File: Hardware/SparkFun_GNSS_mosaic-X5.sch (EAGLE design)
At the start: 68 parts, among them J3 MICROSD, J5 USB Female Type C Connector, U1 MOSAIC-X5X5, U2 SN74AHC1G125DBVR, U5 AP2112K-3.3V

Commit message: Route board.
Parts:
- added R1: 10k, SparkFun-Resistors:10KOHM-0603-1/10W-1%
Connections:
- net PPS_18V renamed PPS_1V8
- new net N$5: J3.DAT3/!CS!, R1.1
- net 3.3V: now also R1.2
- net D+: now also D1.IO4; no longer D1.IO3
- net D-: now also D1.IO3; no longer D1.IO4
- net VIN: now also J7.3; no longer J7.4
- net V_USB: now also J7.4; no longer J7.3
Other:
- note added: "Septentrio mosaic-X5"
- note removed: "Can GP and LOG LEDs be directly driven from module?"
- note removed: "Does the log button have a pull up?"
- moved on the sheet: C1, C18, C19, C20, C3, C4, C5, D10, E1, E2, FB1, J3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

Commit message: Add jumper to ant voltage. Add production panel.
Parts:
- removed C1: 0.1uF, SparkFun-Capacitors:0.1UF-0603-25V-5%
- removed J10: (no value), SparkFun-Connectors:CONN_06NO_SILK_FEMALE_PTH
- removed L1: 39nH, SparkFun-Coils:39NH-0603
- added ANT_V: JUMPER-SMT_3_1-NC_TRACE_SILK, SparkFun-Jumpers:JUMPER-SMT_3_1-NC_TRACE_SILK
- added D2: WHITE, SparkFun-LED:LED-WHITE0603
- added GP2: JUMPER-SMT_2_NC_TRACE_SILK, SparkFun-Jumpers:JUMPER-SMT_2_NC_TRACE_SILK
- added J6: (no value), SparkFun-Connectors:CONN_07NO_SILK
- added Q9: 20V/0.2A/8MHz/1.2Ω/1Vth, SparkFun-DiscreteSemi:MOSFET-NCH-RE1C00UNTL
- added R46, R47: 2.2k, SparkFun-Resistors:2.2KOHM-0603-1/10W-1%
- added R6, R7: 169K, SparkFun-Resistors:169KOHM
- added R9: 1k, SparkFun-Resistors:1KOHM-0603-1/10W-1%
- R11, R4: value 1k -> 2.2k; device SparkFun-Resistors:1KOHM-0603-1/10W-1% -> SparkFun-Resistors:2.2KOHM-0603-1/10W-1%
- R12: value 1k -> 330; device SparkFun-Resistors:1KOHM-0603-1/10W-1% -> SparkFun-Resistors:330OHM-0603-1/10W-1%
- U1: device Septentrio_Mosaic:MOSAIC-X5X5 -> Septentriom_mosaic-X5:MOSAIC-X5X5
- renumbered GP to GP1
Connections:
- net GP_LED renamed PVT_LED
- removed net ANT_VCC: C1.1, L1.2
- new net ANT_V: ANT_V.2, C3.1, FB1.1
- new net ICM-20948-LV_#_1.8V: Q9.G, R46.2
- new net N$6: R6.1, U1.EVENTA
- new net N$7: R7.1, U1.EVENTB
- new net N$8: D2.A, R9.1
- new net N$9: GP2.1, R9.2
- new net PPS_3: Q9.D, R47.1, U2U1.A
- new net RTK_LED: GP2.2, J6.3, U1.GP_LED2
- net 3.3V: now also ANT_V.1, R47.2
- net 5V: now also ANT_V.3; no longer C3.1, FB1.1
- net EVENTA: now also J6.6, R6.2; no longer J10.5, U1.EVENTA
- net EVENTB: now also J6.7, R7.2; no longer J10.6, U1.EVENTB
- net GND: now also D2.C, U1.ANT_2; no longer C1.2
- net GP1: now also J6.1; no longer J10.1
- net GP2: now also J6.2; no longer J10.2
- net GPS_ANT1: no longer L1.1
- net LOG_BTN: now also J6.4; no longer J10.3
- net PPS_1V8: now also Q9.S, R46.1; no longer U2U1.A
- net PPS_3V3: now also J6.5; no longer J10.4
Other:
- note added: "1.8V Input protected by 169k/200k divider"
- note added: "If using single external 3.3V source, move jumper to power antenna with 3.3V."
- note added: "VMax: 6V"
- moved on the sheet: C18, C19, C20, D10, E1, E2, J3, R1, R2, R3, R8, S1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

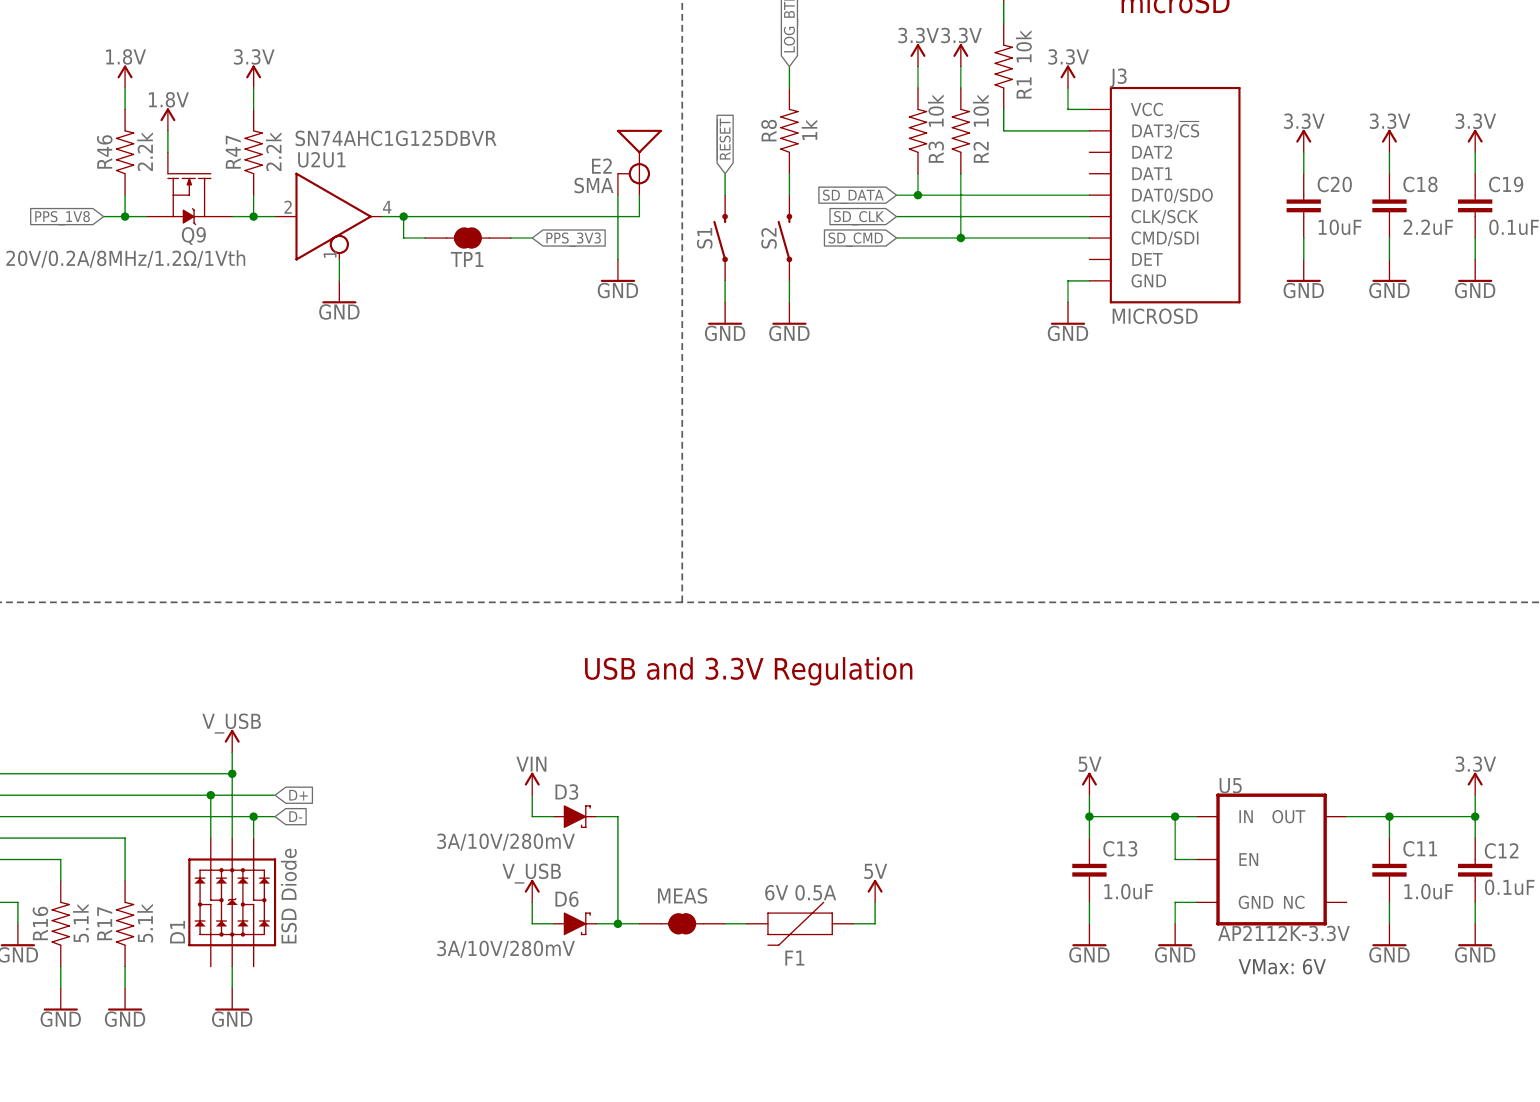
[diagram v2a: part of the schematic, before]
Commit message: Fixed tCream on mosaic pin 1.
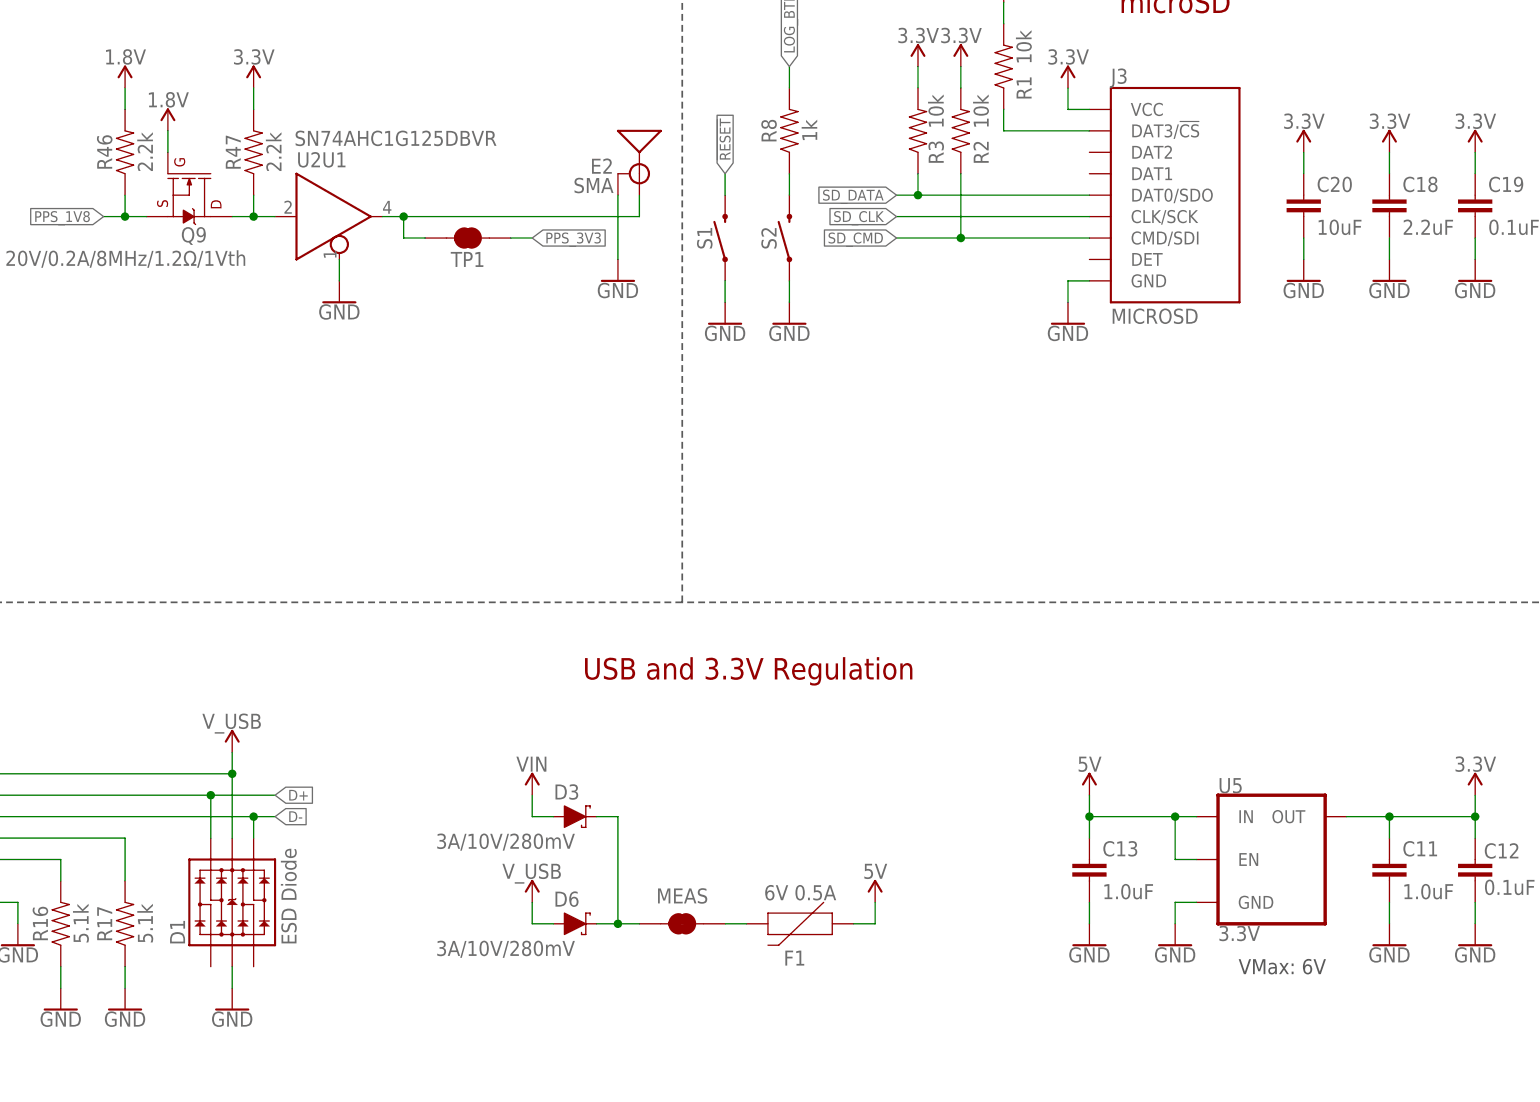
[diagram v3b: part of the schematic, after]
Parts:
- Q9: device SparkFun-DiscreteSemi:MOSFET-NCH-RE1C00UNTL -> SparkFun-DiscreteSemi:MOSFET-NCH-RE1C002UNTCL
- U1: device Septentriom_mosaic-X5:MOSAIC-X5X5 -> Septentrio_mosaic-X5:MOSAIC-X5X5
- U5: value AP2112K-3.3V -> 3.3V

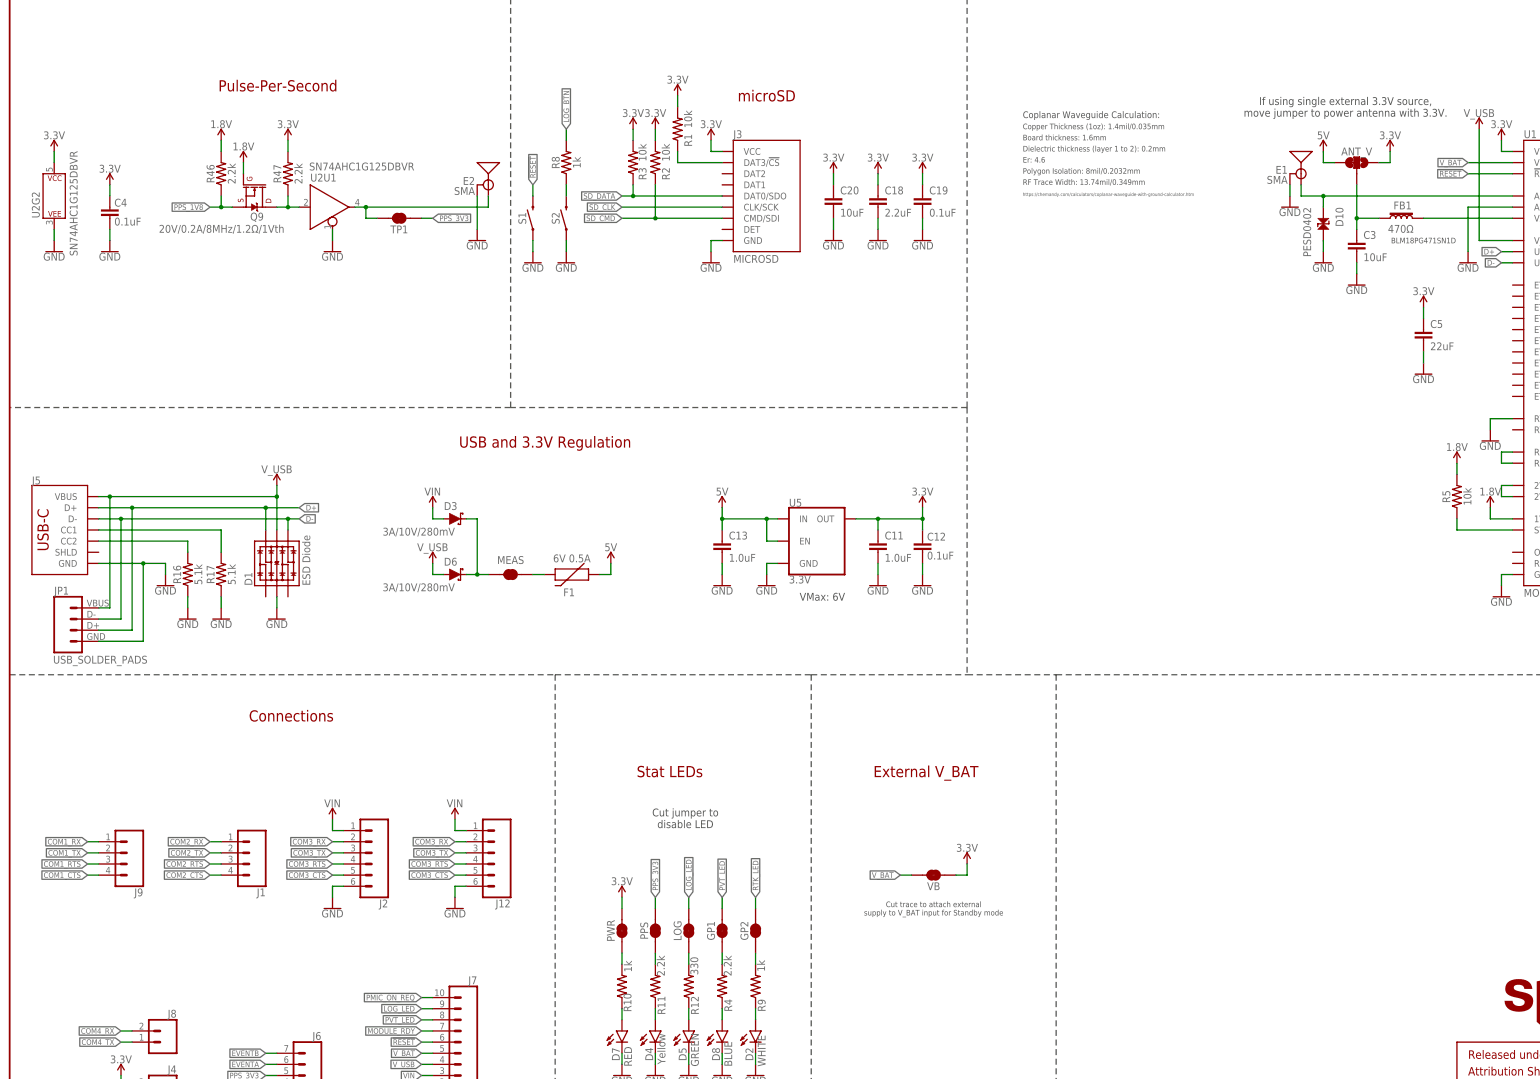
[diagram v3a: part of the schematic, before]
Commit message: Add ESD and USB choke.
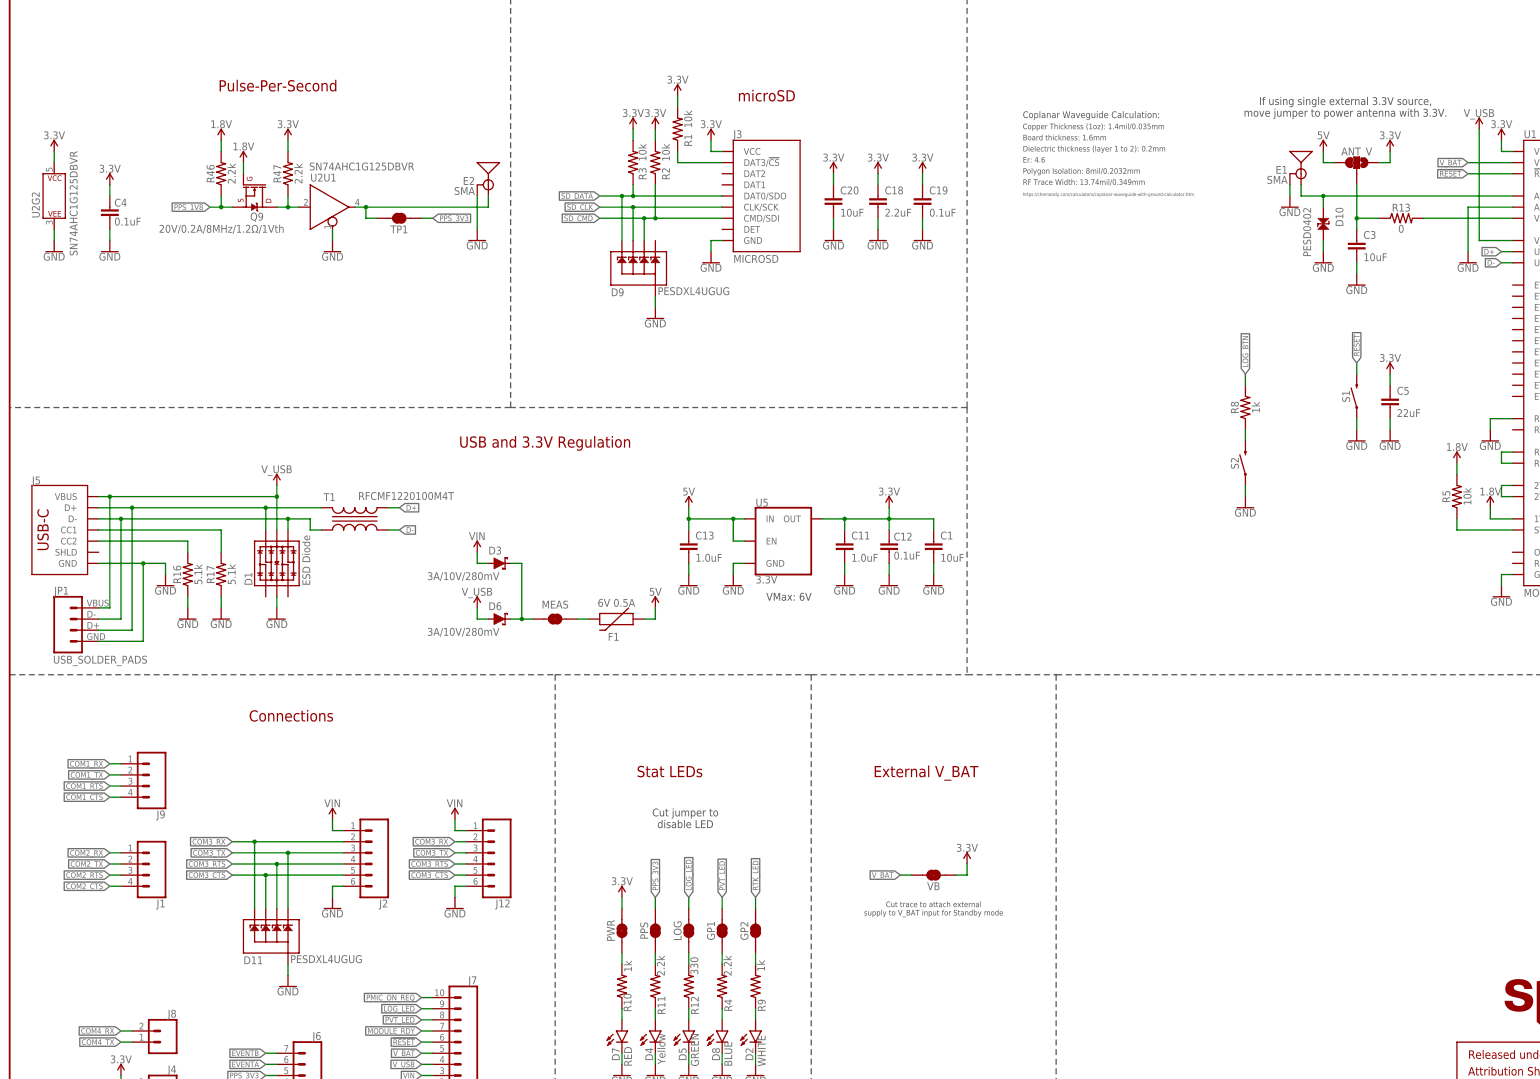
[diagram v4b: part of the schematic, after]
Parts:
- removed FB1: 470Ω, SparkFun-Coils:FERRITE_BEAD-0603-470Ω-100MHZ-1A-200MILIΩ
- added C1: 10uF, SparkFun-Capacitors:10UF-0603-6.3V-20%
- added D11, D9: PESDXL4UGUG, SparkFun-DiscreteSemi:PESDXL4UGUG
- added R13: 0, SparkFun-Resistors:0OHM-0603-1/10W
- added T1: RFCMF1220100M4T, SparkFun-Coils:TRANSFORMER0508
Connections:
- new net USB_D+: D1.IO4, J5.D+, JP1.3, T1.B1
- new net USB_D-: D1.IO3, J5.D-, JP1.2, T1.A1
- net 3.3V: now also C1.1
- net ANT_V: now also R13.1; no longer FB1.1
- net COM3_CTS: now also D11.5
- net COM3_RTS: now also D11.4
- net COM3_RX: now also D11.1
- net COM3_TX: now also D11.3
- net D+: now also T1.B2; no longer D1.IO4, J5.D+, JP1.3
- net D-: now also T1.A2; no longer D1.IO3, J5.D-, JP1.2
- net GND: now also C1.2, D11.2, D9.2
- net SD_CLK: now also D9.5
- net SD_CMD: now also D9.4
- net SD_DATA: now also D9.1
- net VANT: now also R13.2; no longer FB1.2
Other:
- note removed: "BLM18PG471SN1D"
- moved on the sheet: C11, C12, C13, C5, D3, D6, F1, J1, J9, MEAS, R8, S1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
